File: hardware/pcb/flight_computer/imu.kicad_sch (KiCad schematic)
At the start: 3 parts, among them U5 LSM6DSRXTR

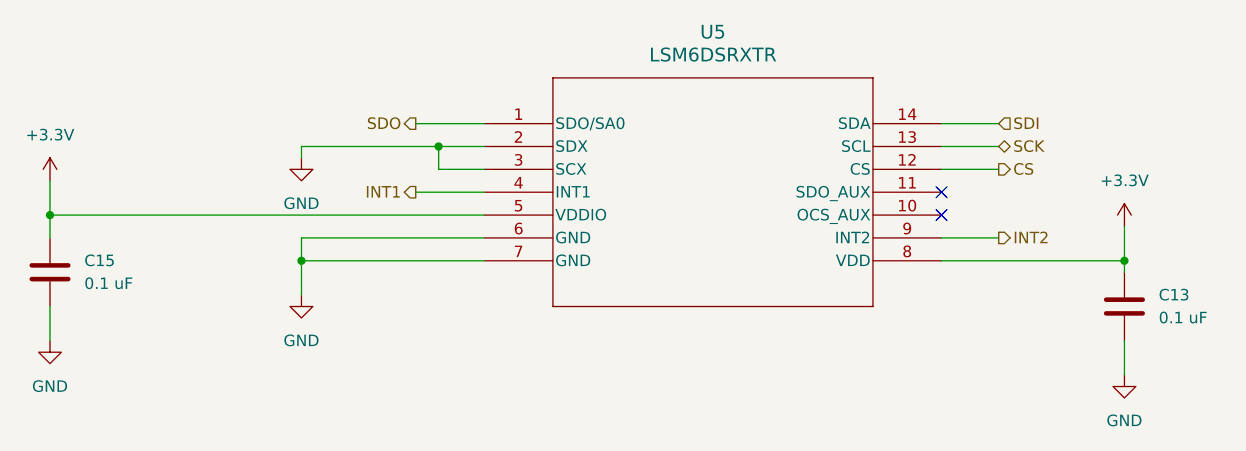
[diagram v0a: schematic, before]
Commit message: Added 3D model
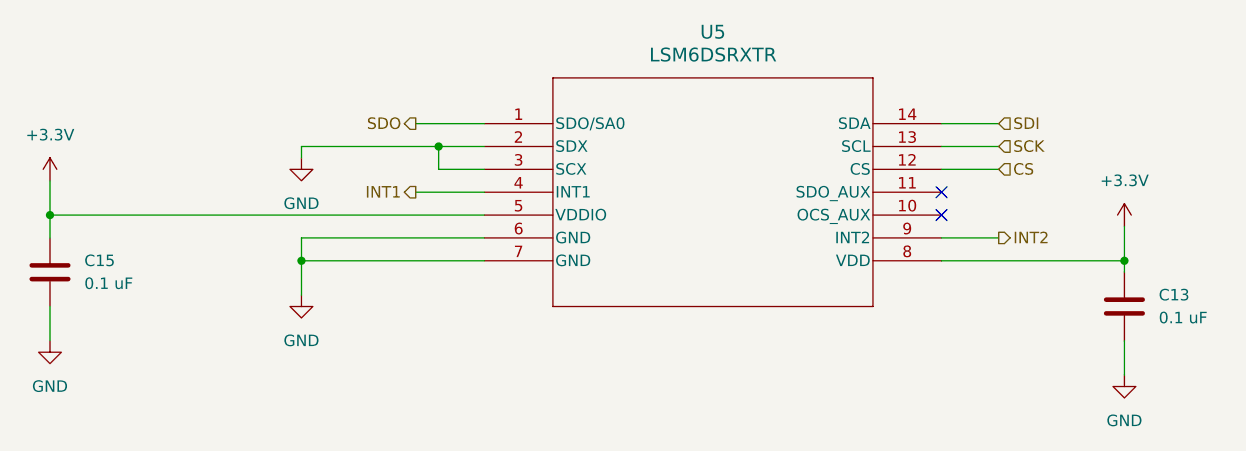
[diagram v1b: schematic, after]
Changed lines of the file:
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@@
 	)
 	(hierarchical_label "SCK"
-		(shape bidirectional)
+		(shape input)
 		(at 194.31 95.25 0)
 		(effects
@@
 	)
 	(hierarchical_label "CS"
-		(shape output)
+		(shape input)
 		(at 194.31 97.79 0)
 		(effects
